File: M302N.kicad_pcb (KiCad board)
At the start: 2 copper layers, 55.2 x 55.2 mm, 6 parts, among them J1 Analog, J2 Digital

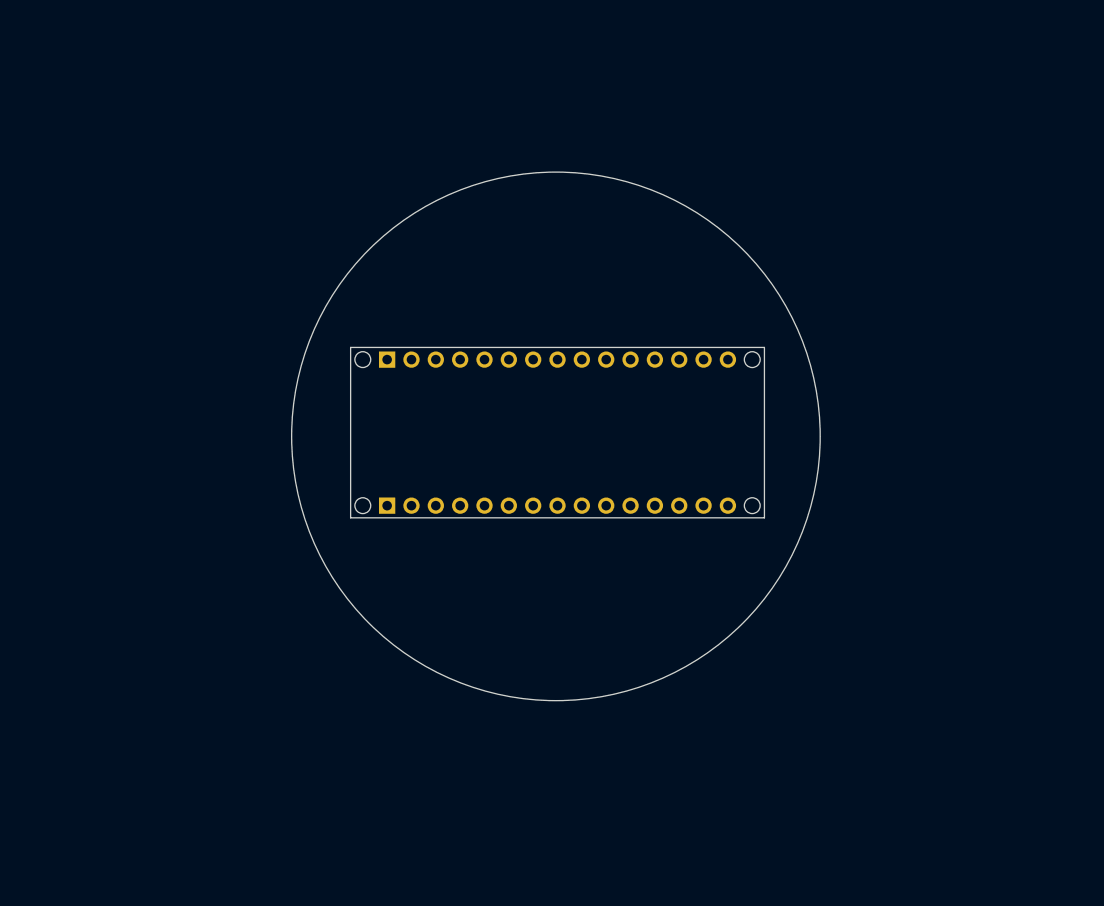
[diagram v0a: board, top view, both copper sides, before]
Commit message: W5500との接続はソケット
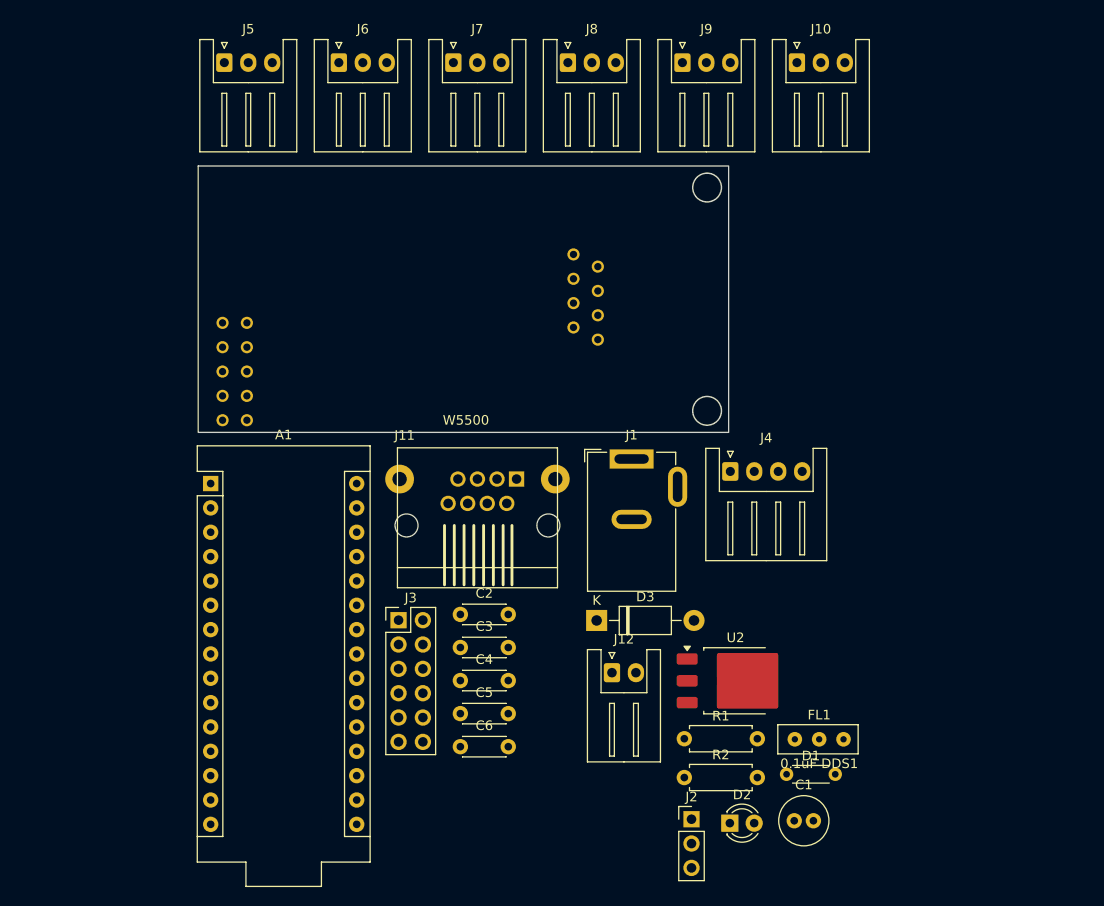
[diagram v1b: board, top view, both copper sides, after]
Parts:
- removed MH1, MH2, MH3, MH4: MountingHole_65mil, Arduino_MountingHole:MountingHole_65mil
- added A1: Arduino_Nano_v3.x, Arduino:Arduino_Nano, F.Cu at (85.4, 96.4)
- added C1: 100uF/25V, Capacitor_THT:C_Radial_D5.0mm_H11.0mm_P2.00mm, F.Cu at (146.3, 131.6)
- added C2: 0.1uF, Capacitor_THT:C_Disc_D4.3mm_W1.9mm_P5.00mm, F.Cu at (111.5, 110.1)
- added C3: 0.1uF, Capacitor_THT:C_Disc_D4.3mm_W1.9mm_P5.00mm, F.Cu at (111.5, 113.5)
- added C4: 0.1uF, Capacitor_THT:C_Disc_D4.3mm_W1.9mm_P5.00mm, F.Cu at (111.5, 117.0)
- added C5: 0.1uF, Capacitor_THT:C_Disc_D4.3mm_W1.9mm_P5.00mm, F.Cu at (111.5, 120.4)
- added C6: 0.1uF, Capacitor_THT:C_Disc_D4.3mm_W1.9mm_P5.00mm, F.Cu at (111.5, 123.9)
- added D1: 1S4, Resistor_THT:R_Axial_DIN0204_L3.6mm_D1.6mm_P5.08mm_Horizontal, F.Cu at (145.5, 126.8)
- added D2: LED, LED_THT:LED_D3.0mm, F.Cu at (139.6, 131.9)
- added D3: 1N4001, Diode_THT:D_DO-41_SOD81_P10.16mm_Horizontal, F.Cu at (125.7, 110.7)
- added FL1: 0.1uF DDS1, HOLLY2:DSS1, F.Cu at (148.9, 123.1)
- added J10: ADC_IN, Connector_JST:JST_XH_S3B-XH-A_1x03_P2.50mm_Horizontal, F.Cu at (146.6, 52.5)
- added J11: RJ45, HOLLY2:RJ45_Neltron_7810-8P8C, F.Cu at (113.2, 100.8)
- added J12: DC12V FAN, Connector_JST:JST_XH_S2B-XH-A_1x02_P2.50mm_Horizontal, F.Cu at (127.3, 116.2)
- added J3: extend I/O, Connector_PinHeader_2.54mm:PinHeader_2x06_P2.54mm_Vertical, F.Cu at (105.0, 110.7)
- added J4: I2C-1, Connector_JST:JST_XH_S4B-XH-A_1x04_P2.50mm_Horizontal, F.Cu at (139.6, 95.2)
- added J5: ADC_IN, Connector_JST:JST_XH_S3B-XH-A_1x03_P2.50mm_Horizontal, F.Cu at (86.8, 52.5)
- added J6: ADC_IN, Connector_JST:JST_XH_S3B-XH-A_1x03_P2.50mm_Horizontal, F.Cu at (98.8, 52.5)
- added J7: ADC_IN, Connector_JST:JST_XH_S3B-XH-A_1x03_P2.50mm_Horizontal, F.Cu at (110.7, 52.5)
- added J8: ADC_IN, Connector_JST:JST_XH_S3B-XH-A_1x03_P2.50mm_Horizontal, F.Cu at (122.7, 52.5)
- added J9: ADC_IN, Connector_JST:JST_XH_S3B-XH-A_1x03_P2.50mm_Horizontal, F.Cu at (134.6, 52.5)
- added R1: 510, Resistor_THT:R_Axial_DIN0207_L6.3mm_D2.5mm_P7.62mm_Horizontal, F.Cu at (134.8, 123.0)
- added R2: 10k, Resistor_THT:R_Axial_DIN0207_L6.3mm_D2.5mm_P7.62mm_Horizontal, F.Cu at (134.8, 127.1)
- added U1: W5500, HOLLY2:W5500LARGE, F.Cu at (84.1, 91.1)
- added U2: NJM2845DL1-05, HOLLY2:NJM2845, F.Cu at (140.2, 117.0)
- J1: value Analog -> DC12V; footprint Connector_PinHeader_2.54mm:PinHeader_1x15_P2.54mm_Vertical -> Connector_BarrelJack:BarrelJack_GCT_DCJ200-10-A_Horizontal; moved to F.Cu
- J2: value Digital -> UART; footprint Connector_PinHeader_2.54mm:PinHeader_1x15_P2.54mm_Vertical -> Connector_PinHeader_2.54mm:PinHeader_1x03_P2.54mm_Vertical; moved to F.Cu
- moved J2 57.5 mm to (135.6, 131.4), turned to 0 degrees
- moved J1 26.0 mm to (129.3, 93.9), turned to 0 degrees
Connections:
- J1 pad 1: /D13/SCK -> /+12V
- J1 pad 2: +3V3 -> Net-(J1-Pad2)
- J1 pad 3: /AREF -> GND
- J2 pad 1: /D12/MISO -> GND
- J2 pad 2: /*D11/MOSI -> Net-(A1-D0/RX)
- J2 pad 3: /*D10/SS -> Net-(A1-D1/TX)
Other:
- board size 55.2 x 55.2 mm -> 55.3 x 27.8 mm
- board text removed: "ICSP"
- board text removed: "USB Mini-B"

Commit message: PCB設計途中
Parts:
- removed J6, J7: ADC_IN, Connector_JST:JST_XH_S3B-XH-A_1x03_P2.50mm_Horizontal
- removed U2: NJM2845DL1-05, HOLLY2:NJM2845
- added J13: Conn_01x05_Socket, Connector_PinSocket_2.54mm:PinSocket_1x05_P2.54mm_Vertical, F.Cu at (159.7, 112.7)
- added J14: Conn_01x05_Socket, Connector_PinSocket_2.54mm:PinSocket_1x05_P2.54mm_Vertical, F.Cu at (164.3, 112.7)
- added J18: Conn_01x04_Socket, Connector_PinSocket_2.54mm:PinSocket_1x04_P2.54mm_Vertical, F.Cu at (128.8, 69.8)
- added J19: Conn_01x04_Socket, Connector_PinSocket_2.54mm:PinSocket_1x04_P2.54mm_Vertical, F.Cu at (131.9, 71.4)
- added SW1: SW_Reed, HOLLY:REED_SW, F.Cu at (166.6, 98.4)
- A1: footprint Arduino:Arduino_Nano -> Module:Arduino_Nano
- moved J10 80.1 mm to (85.2, 103.9)
- moved D2 70.7 mm to (74.9, 103.1), turned to 90 degrees
- moved J4 70.6 mm to (74.9, 66.8), turned to -90 degrees
- moved FL1 61.0 mm to (155.4, 62.5), turned to 180 degrees
- moved J8 57.7 mm to (85.3, 96.5)
- moved J12 57.7 mm to (74.8, 92.3), turned to -90 degrees
- moved J9 56.8 mm to (98.3, 96.3)
- moved J2 56.2 mm to (167.4, 85.1)
- moved J3 47.5 mm to (152.5, 112.7)
- moved A1 37.5 mm to (120.4, 110.0), turned to 90 degrees
- moved D3 33.8 mm to (158.3, 102.1)
- moved R1 33.5 mm to (168.1, 126.0)
- moved R2 33.5 mm to (168.1, 130.0)
- moved C2 32.2 mm to (143.6, 112.1)
- moved C3 32.2 mm to (143.6, 115.6)
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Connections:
- A1 pad 13: /*D10/SS -> Net-(A1-D10)
- A1 pad 14: /*D11/MOSI -> Net-(A1-D11)
- A1 pad 15: /D12/MISO -> Net-(A1-D12)
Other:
- board size 55.3 x 27.8 mm -> 100.1 x 56 mm

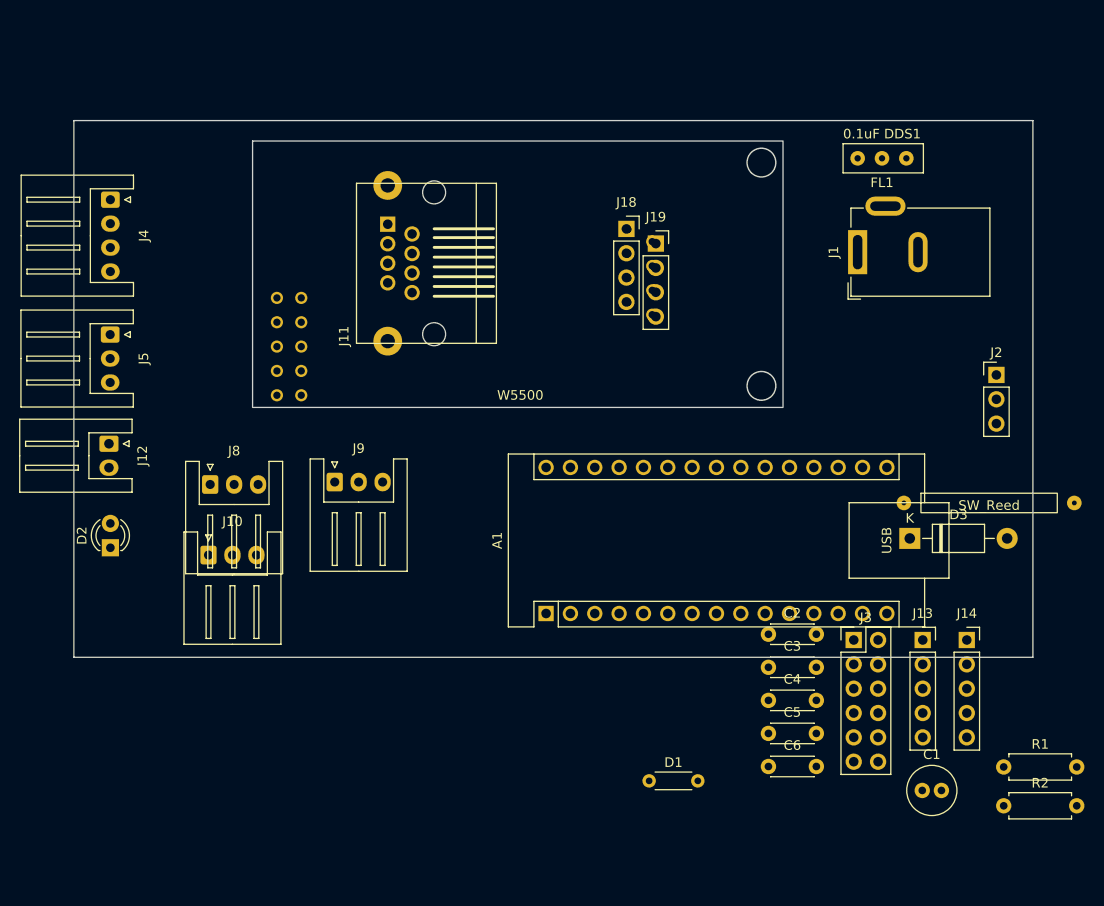
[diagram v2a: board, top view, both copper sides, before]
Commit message: PCB設計とRJ45モジュラー
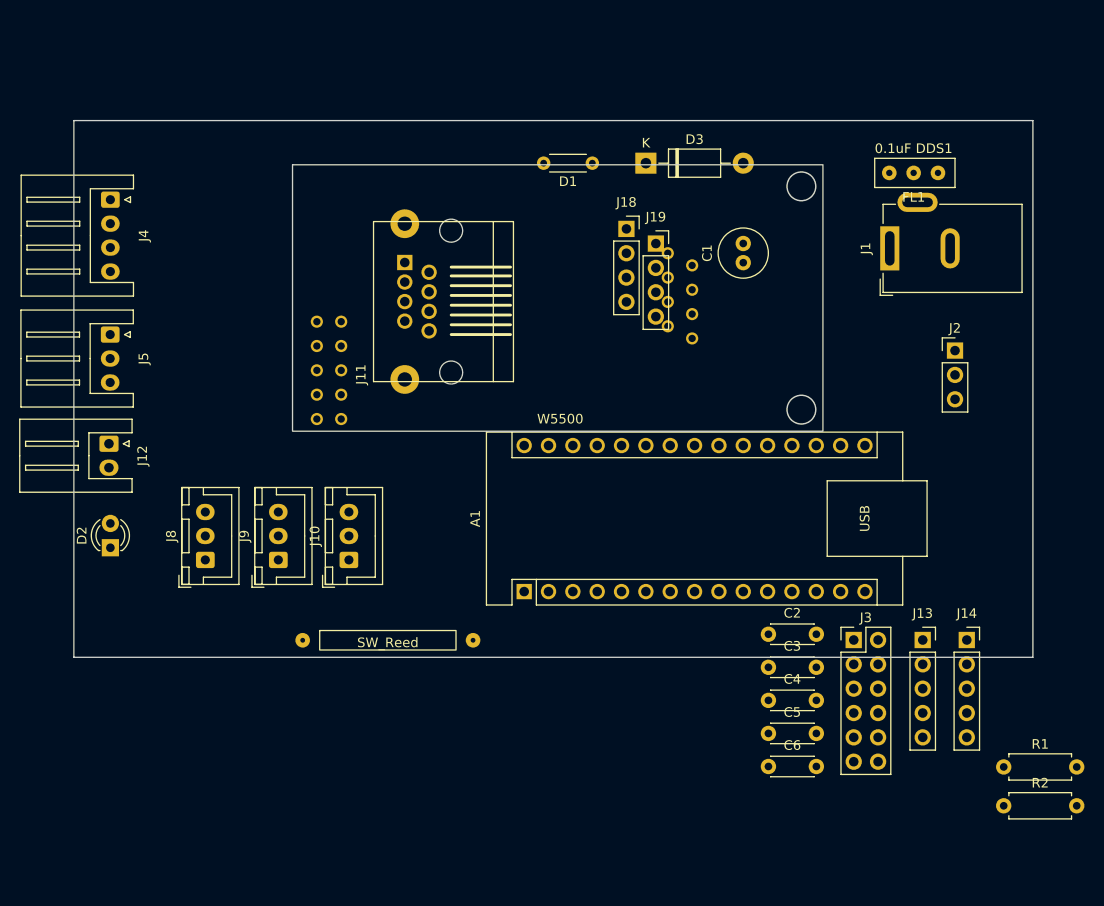
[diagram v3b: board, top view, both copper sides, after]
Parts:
- J10, J8, J9: footprint Connector_JST:JST_XH_S3B-XH-A_1x03_P2.50mm_Horizontal -> Connector_JST:JST_XH_B3B-XH-A_1x03_P2.50mm_Vertical
- moved D1 64.7 mm to (125.2, 63.0), turned to 180 degrees
- moved SW1 64.4 mm to (103.9, 112.8)
- moved C1 58.2 mm to (141.0, 73.4), turned to 90 degrees
- moved D3 47.9 mm to (130.8, 63.0)
- moved J10 14.7 mm to (99.8, 104.4), turned to 90 degrees
- moved J9 10.0 mm to (92.5, 104.4), turned to 90 degrees
- moved J8 7.89 mm to (84.8, 104.4), turned to 90 degrees
- moved J2 5.01 mm to (163.1, 82.5)
- moved U1 4.85 mm to (93.9, 91.0)
- moved J11 4.37 mm to (110.5, 77.4)
- moved FL1 3.64 mm to (158.8, 64.0)
- moved J1 3.38 mm to (156.3, 71.9)
- moved A1 3.23 mm to (118.1, 107.7)

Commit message: PCB設計中
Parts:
- removed U1: W5500, HOLLY2:W5500LARGE
- added R3: TNR10V471K, Varistor:RV_Disc_D12mm_W3.9mm_P7.5mm, F.Cu at (105.6, 85.5)
- added U2: NJM2845DL1-05, Package_TO_SOT_SMD:TO-252-3_TabPin2, F.Cu at (126.7, 63.9)
- J1, J2: moved to B.Cu
- moved R1 90.7 mm to (78.8, 110.3)
- moved C6 74.9 mm to (93.5, 70.2), turned to 180 degrees
- moved J14 71.6 mm to (96.5, 89.7), turned to 180 degrees
- moved FL1 68.5 mm to (91.0, 74.0)
- moved R2 68.4 mm to (102.8, 110.0), turned to 180 degrees
- moved C4 67.4 mm to (80.5, 95.2), turned to 90 degrees
- moved J13 64.9 mm to (99.1, 89.7), turned to 180 degrees
- moved C5 61.5 mm to (134.2, 61.7), turned to -90 degrees
- moved C3 55.5 mm to (118.5, 66.1), turned to 180 degrees
- moved C2 55.3 mm to (118.5, 62.9), turned to 180 degrees
- moved D3 54.7 mm to (85.9, 94.2), turned to 90 degrees
- moved J3 48.2 mm to (108.2, 93.7)
- moved C1 33.4 mm to (108.4, 66.1)
- moved D1 25.8 mm to (101.9, 74.0), turned to 0 degrees
- moved J2 13.9 mm to (159.1, 95.8), turned to 180 degrees
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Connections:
- net Net-(A1-D10) renamed /*D10/SS
- net Net-(A1-D11) renamed /*D11/MOSI
- net Net-(A1-D12) renamed /D12/MISO
- J11 pad 2: Net-(J18-Pin_2) -> Net-(J19-Pin_1)
- J11 pad 3: Net-(J18-Pin_3) -> Net-(J18-Pin_2)
- J11 pad 6: Net-(J19-Pin_2) -> Net-(J19-Pin_3)
- J18 pad 3: Net-(J18-Pin_3) -> unconnected-(J18-Pin_3-Pad3)
- J19 pad 1: unconnected-(J19-Pin_1-Pad1) -> Net-(J19-Pin_1)
- J19 pad 2: Net-(J19-Pin_2) -> unconnected-(J19-Pin_2-Pad2)
- J19 pad 3: unconnected-(J19-Pin_3-Pad3) -> Net-(J19-Pin_3)

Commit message: PCB継続
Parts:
- added U1: W5500, HOLLY2:W5500LARGE, F.Cu at (93.8, 91.0)
- moved J3 15.5 mm to (117.9, 105.8), turned to 180 degrees
- moved R2 11.9 mm to (106.0, 98.6), turned to -90 degrees
- moved D3 10.2 mm to (85.9, 84.1), turned to -90 degrees
- moved C6 6.41 mm to (88.1, 66.8)
- moved FL1 6.25 mm to (85.3, 71.4)
- moved SW1 1.02 mm to (102.9, 112.8), turned to 180 degrees
- moved C4 0.43 mm to (80.5, 94.8), turned to -90 degrees
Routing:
- net /+12V: track 0.00 -> 136.8 mm
- net +5V: track 0.00 -> 121.0 mm
- net /*D3: track 0.00 -> 76.1 mm, vias 0 -> 1
- net Net-(A1-A7): track 0.00 -> 72.8 mm
- net Net-(J1-Pad2): track 0.00 -> 67.8 mm
- net Net-(U2-Vin): track 0.00 -> 58.5 mm
- net /~{RESET}: track 0.00 -> 51.8 mm, vias 0 -> 1
- net Net-(A1-D9): track 0.00 -> 41.5 mm
- net Net-(A1-D8): track 0.00 -> 40.6 mm, vias 0 -> 3
- net Net-(A1-D0/RX): track 0.00 -> 39.2 mm, vias 0 -> 1
- net Net-(A1-D1/TX): track 0.00 -> 39.1 mm, vias 0 -> 1
- net Net-(A1-D4): track 0.00 -> 36.6 mm, vias 0 -> 3
- net Net-(A1-D5): track 0.00 -> 36.6 mm, vias 0 -> 3
- net Net-(A1-D6): track 0.00 -> 36.2 mm, vias 0 -> 3
- net Net-(A1-D7): track 0.00 -> 36.1 mm, vias 0 -> 3
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- added copper zone on B.Cu, net GND

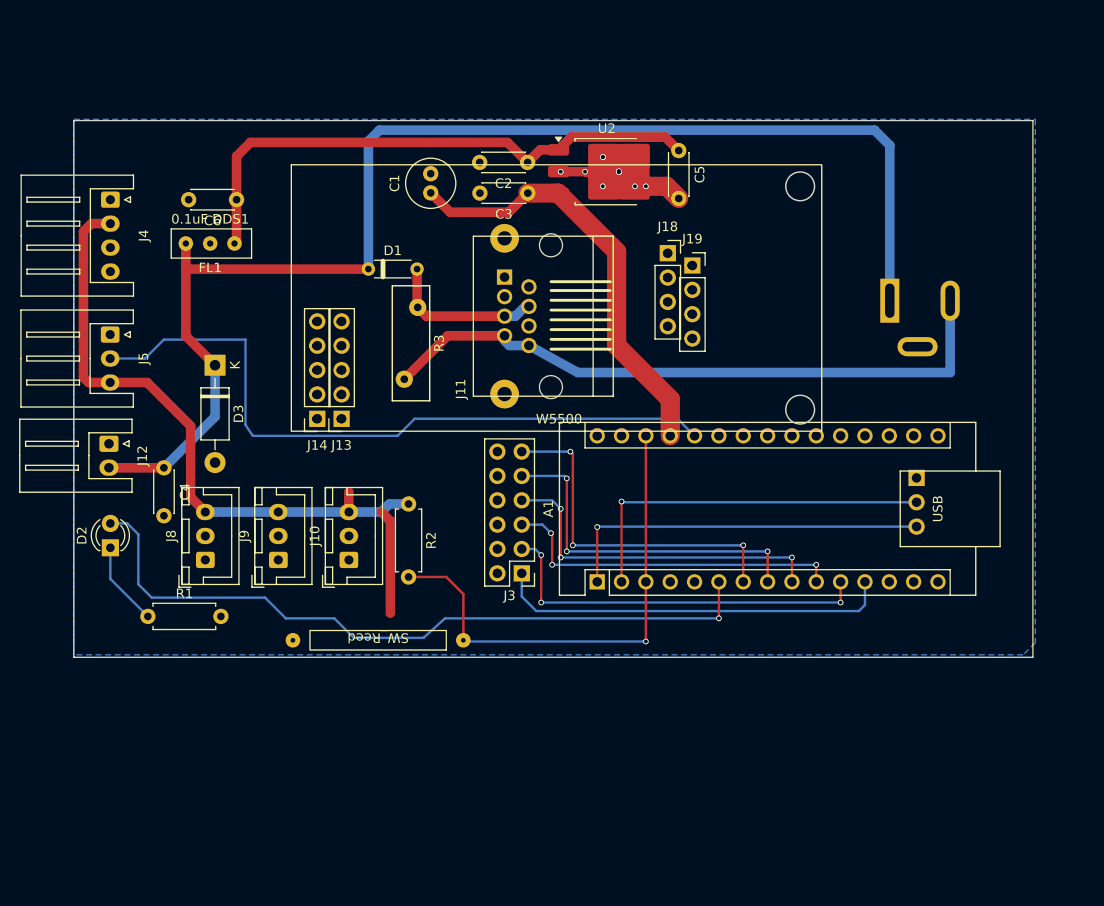
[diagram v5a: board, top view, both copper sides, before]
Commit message: PCB基本完成・文字入れなど未完
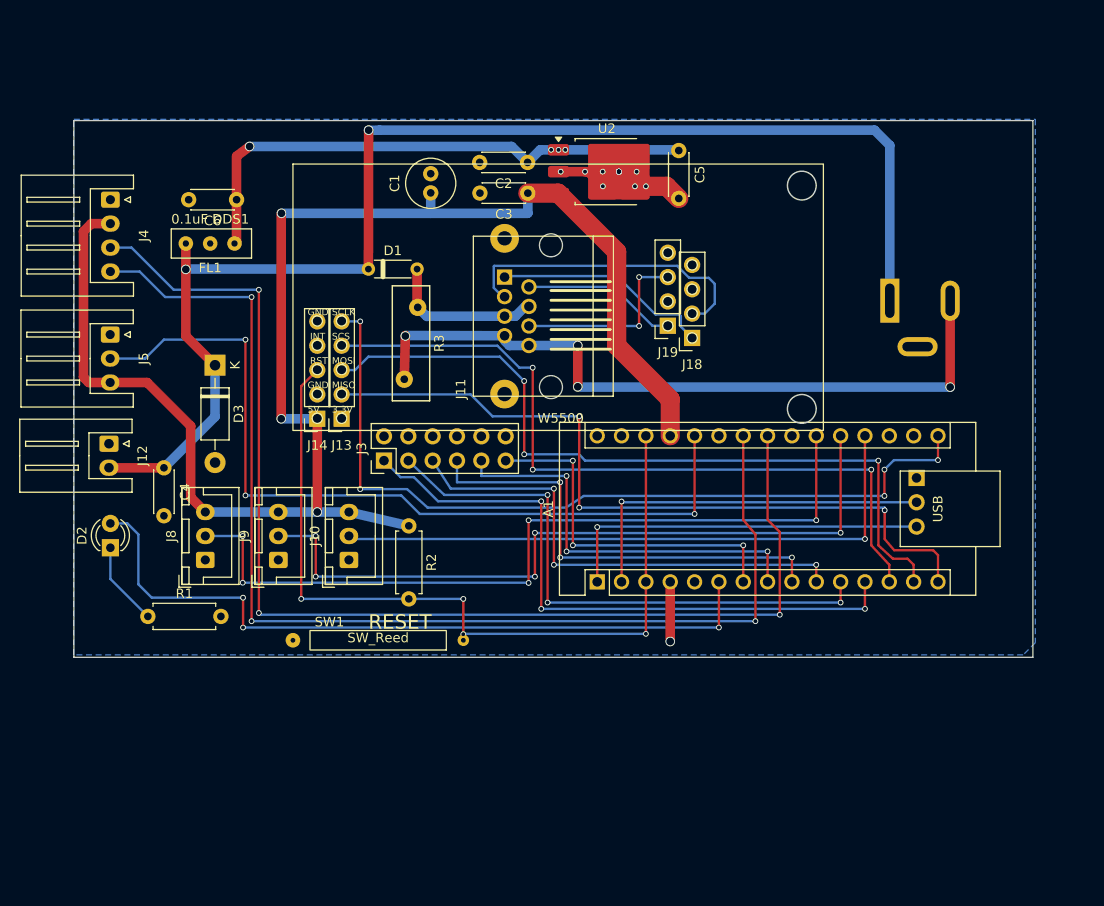
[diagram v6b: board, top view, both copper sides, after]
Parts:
- moved J3 18.6 mm to (103.5, 94.0), turned to 90 degrees
- moved J18 9.20 mm to (135.6, 81.2), turned to 180 degrees
- moved J19 6.79 mm to (133.1, 80.0), turned to 180 degrees
- moved R2 2.29 mm to (106.1, 100.8)
- moved U1 0.19 mm to (94.0, 90.9)
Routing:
- net /A4/SDA: track 0.00 -> 124.7 mm, vias 0 -> 3
- net /A5/SCL: track 0.00 -> 122.0 mm, vias 0 -> 3
- net Net-(A1-D13): track 0.00 -> 86.5 mm, vias 0 -> 5
- net Net-(A1-A2): track 0.00 -> 83.9 mm, vias 0 -> 5
- net /*D11/MOSI: track 0.00 -> 80.7 mm, vias 0 -> 3
- net /D12/MISO: track 0.00 -> 79.5 mm, vias 0 -> 3
- net /*D10/SS: track 0.00 -> 79.3 mm, vias 0 -> 3
- net Net-(A1-A1): track 0.00 -> 77.6 mm, vias 0 -> 5
- net Net-(A1-A0): track 0.00 -> 65.0 mm, vias 0 -> 1
- net +5V: track 121.0 -> 160.8 mm, vias 0 -> 3
- net /~{RESET}: track 51.8 -> 85.7 mm, vias 1 -> 4
- net Net-(J18-Pin_2): track 0.00 -> 32.5 mm
- net Net-(A1-D9): track 41.5 -> 66.0 mm, vias 0 -> 3
- net Net-(J18-Pin_1): track 0.00 -> 22.9 mm
- net Net-(J19-Pin_3): track 0.00 -> 19.6 mm, vias 0 -> 2
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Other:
- board text added: "RESET"
